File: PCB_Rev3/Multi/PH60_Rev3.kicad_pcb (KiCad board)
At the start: 2 copper layers, 285 x 94.6 mm, 213 parts, among them J1 Conn_01x02_Pin, J2 Conn_01x02_Pin, J3 USB_C_Receptacle_USB2.0_16P, J4 Conn_01x04_Socket, U1 TP4057, U2 nRF52840, U4 TPS2116DRL, X1 32.768kHz, X2 Crystal_Generic

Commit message: Merge changes
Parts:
- removed J4: Conn_01x04_Socket, Connector_Molex:Molex_Pico-EZmate_78171-0004_1x04-1MP_P1.20mm_Vertical
- removed REF**: Stabilizer_Cherry_MX_2.00u, PCM_Mounting_Keyboard_Stabilizer:Stabilizer_Cherry_MX_2.00u
- removed S61-1: MX1A, PCM_Switch_Keyboard_Hotswap_Kailh:SW_Hotswap_Kailh_MX_Plated_1.50u
- added S55-x1: MX_stab, PCM_Mounting_Keyboard_Stabilizer:Stabilizer_Cherry_MX_2.00u, F.Cu at (288.1, 95.2)
- moved D16 13.2 mm to (39.6, 61.6), turned to 90 degrees
- moved R4 9.30 mm to (36.7, 69.3), turned to 90 degrees
- moved C12 4.79 mm to (48.8, 68.0), turned to 180 degrees
- moved AE1 2.92 mm to (36.7, 70.1)
- moved S61 2.38 mm to (233.4, 114.3)
- moved J2 0.95 mm to (148.2, 113.9), turned to 90 degrees
- moved C13 0.21 mm to (50.2, 68.5), turned to -90 degrees
- moved L3 0.09 mm to (48.8, 69.0)
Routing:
- net col_0: track 129.2 -> 208.9 mm, vias 1 -> 5
- net Net-(D64-A): track 28.5 -> 6.18 mm
- net col_10: track 287.9 -> 273.3 mm
- net Net-(D67-A): track 19.1 -> 30.4 mm
- net Net-(D62-A): track 40.5 -> 50.9 mm
- net Net-(AE1-A): track 10.4 -> 0.00 mm
- net Net-(C12-Pad2): track 3.89 -> 12.6 mm
- net row_1: track 309.0 -> 301.3 mm, vias 17 -> 16
- net Net-(D63-A): track 21.2 -> 25.6 mm
- net GND: track 23.7 -> 27.1 mm, vias 117 -> 163
- net row_0: track 308.7 -> 306.5 mm
- net col_2: track 138.3 -> 136.9 mm
- net col_6: track 231.3 -> 232.6 mm
- net col_8: track 260.8 -> 262.1 mm
- net /RESET: track 138.7 -> 139.5 mm
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
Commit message: Wires change
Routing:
- net Net-(D59-A): track 23.9 -> 43.5 mm, vias 1 -> 0
- net col_0: track 208.9 -> 220.7 mm
- net Net-(D58-A): track 13.5 -> 22.2 mm
- net col_1: track 112.6 -> 105.9 mm
- net Net-(D60-A): track 26.4 -> 30.9 mm, vias 1 -> 0
- net GND: vias 163 -> 165

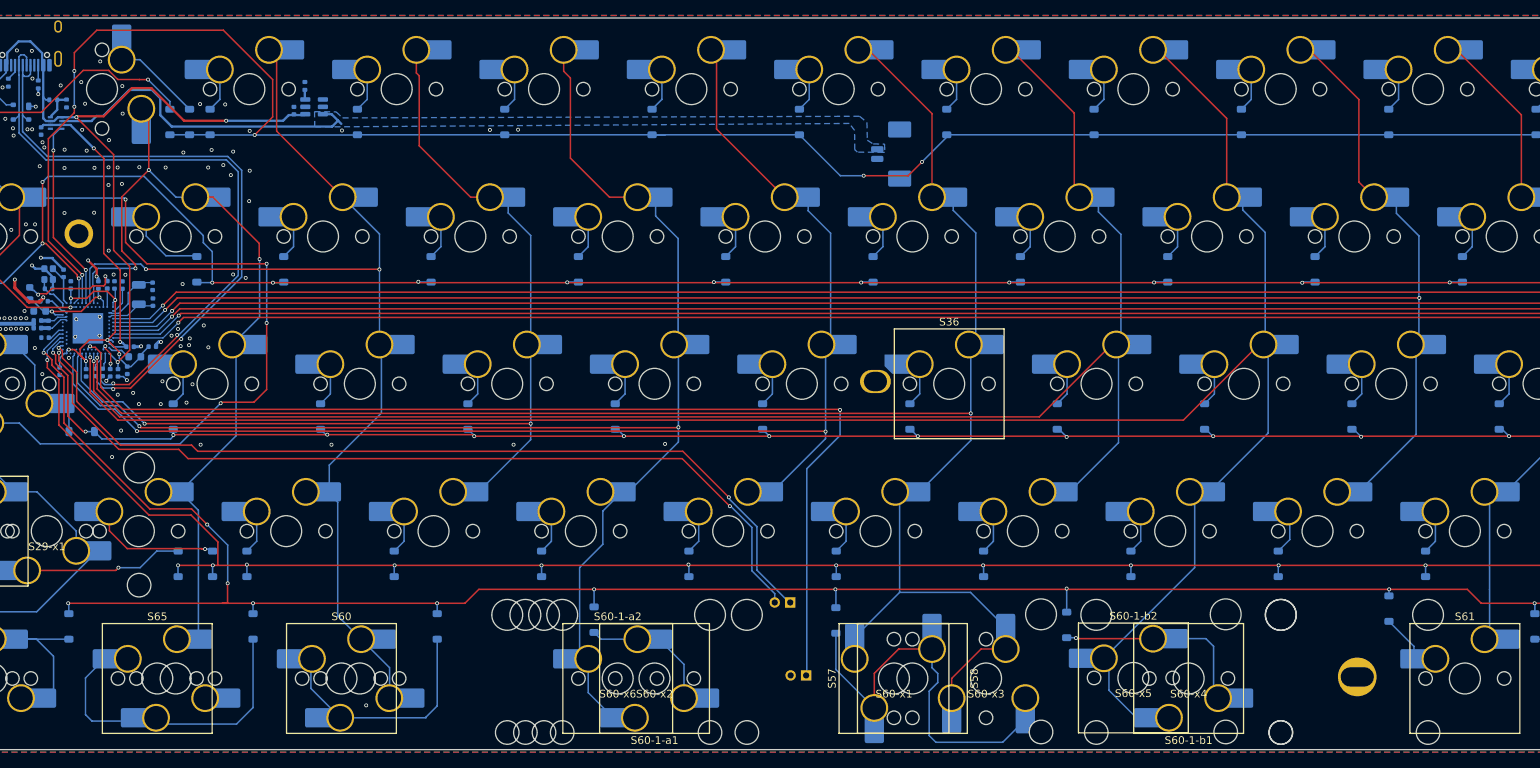
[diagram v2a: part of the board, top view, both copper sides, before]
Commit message: multi电池段子位置调整
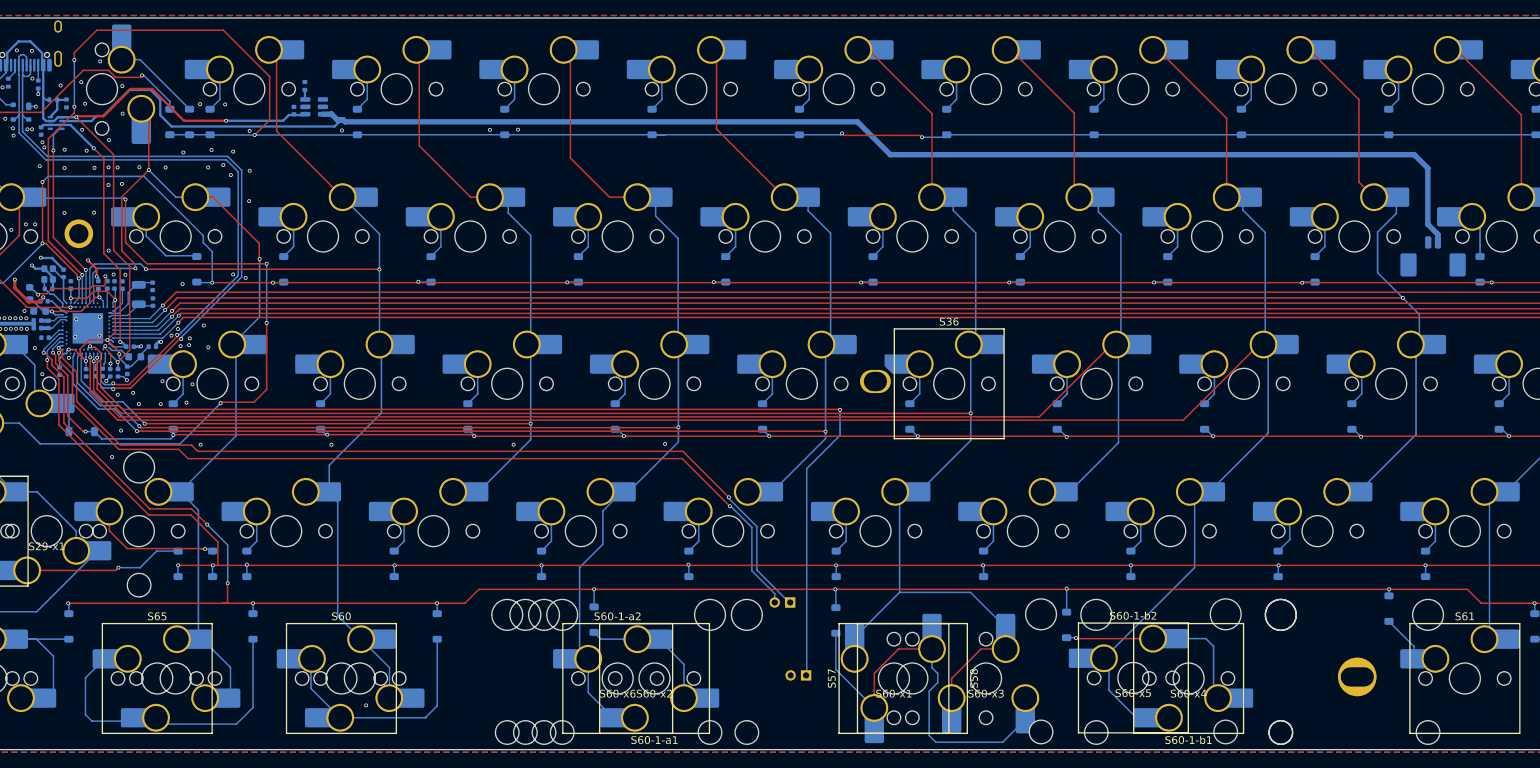
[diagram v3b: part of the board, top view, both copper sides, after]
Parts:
- moved BT1 70.8 mm to (229.2, 60.3), turned to 180 degrees
- moved D26 2.28 mm to (235.3, 61.4)
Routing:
- net +BATT: track 43.8 -> 198.0 mm
- net col_1: track 105.9 -> 114.5 mm
- net row_0: track 306.5 -> 302.1 mm
- net col_10: track 273.3 -> 270.1 mm
- net Net-(D59-A): track 43.5 -> 41.7 mm
- net Net-(D26-A): track 5.67 -> 4.13 mm
- net col_4: track 182.0 -> 180.7 mm
- net Net-(D58-A): track 22.2 -> 21.0 mm
- net col_9: track 233.5 -> 232.8 mm
- net col_3: track 129.3 -> 128.8 mm
- removed copper zone on B.Cu, net +BATT
